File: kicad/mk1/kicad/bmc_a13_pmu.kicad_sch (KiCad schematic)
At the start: 55 parts, among them SW3 PWR_BUT, U25 SY8008A, U26 SY8008A, U3 AXP209

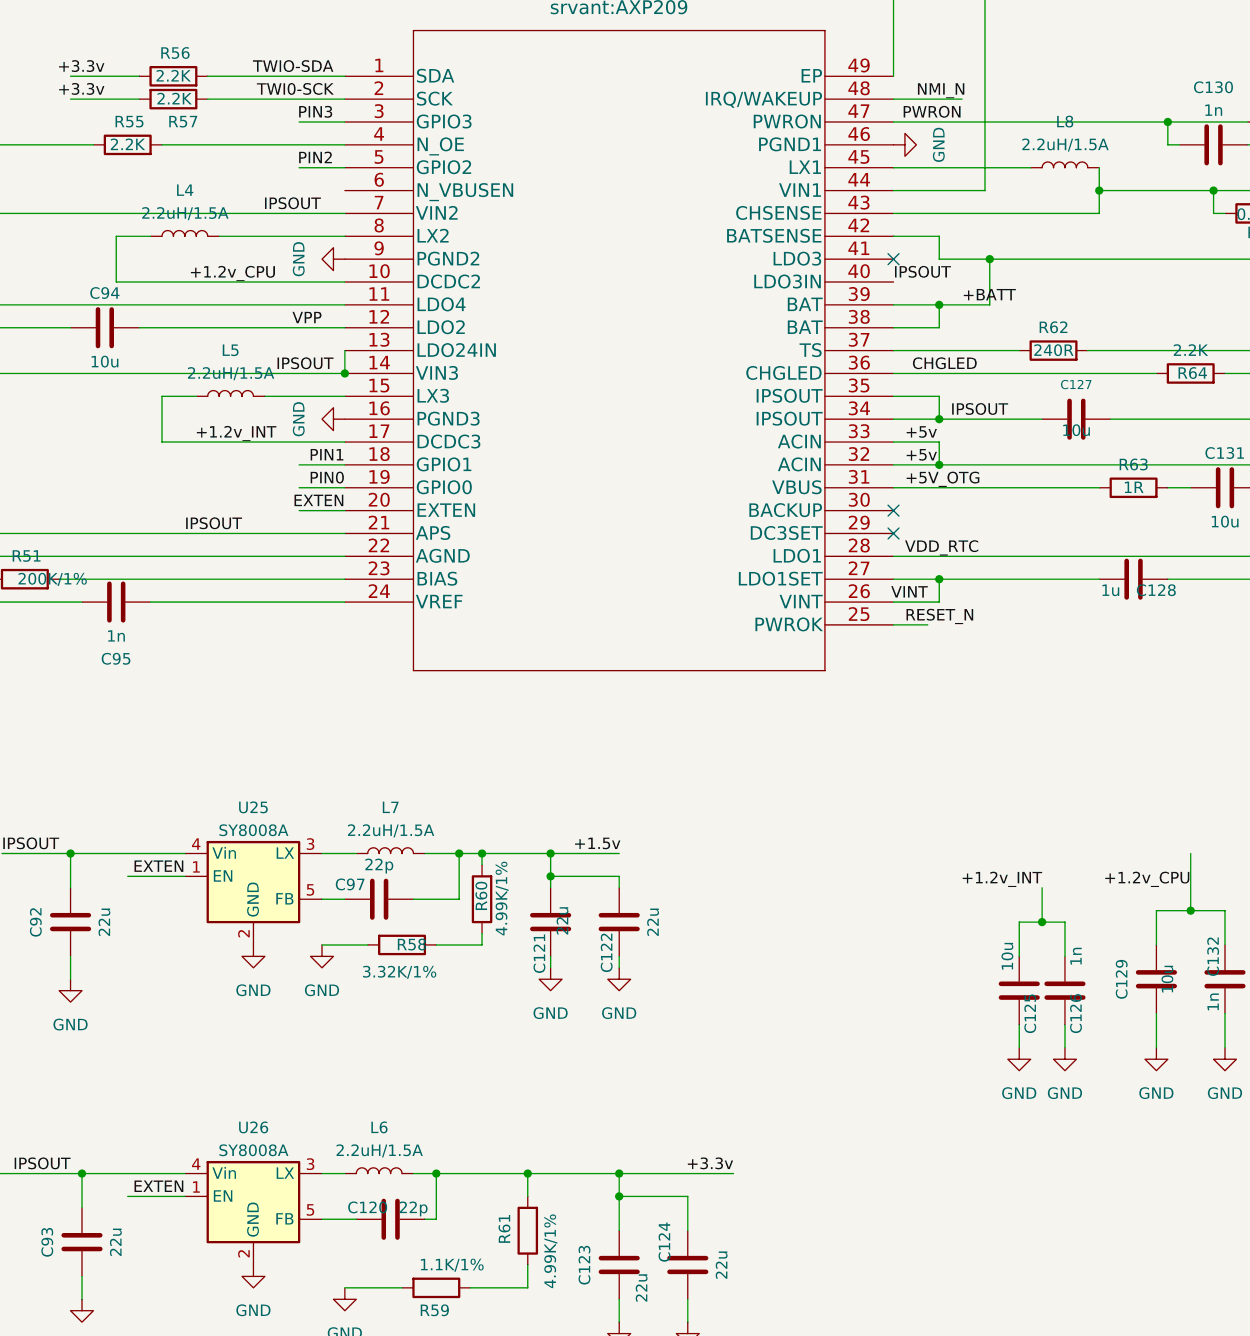
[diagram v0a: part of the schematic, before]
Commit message: work on schematics
* add power rail
* import CM4 related part
* design most of the BMC-PHY part
* create new library/footprint for rp t113-s3 SOM
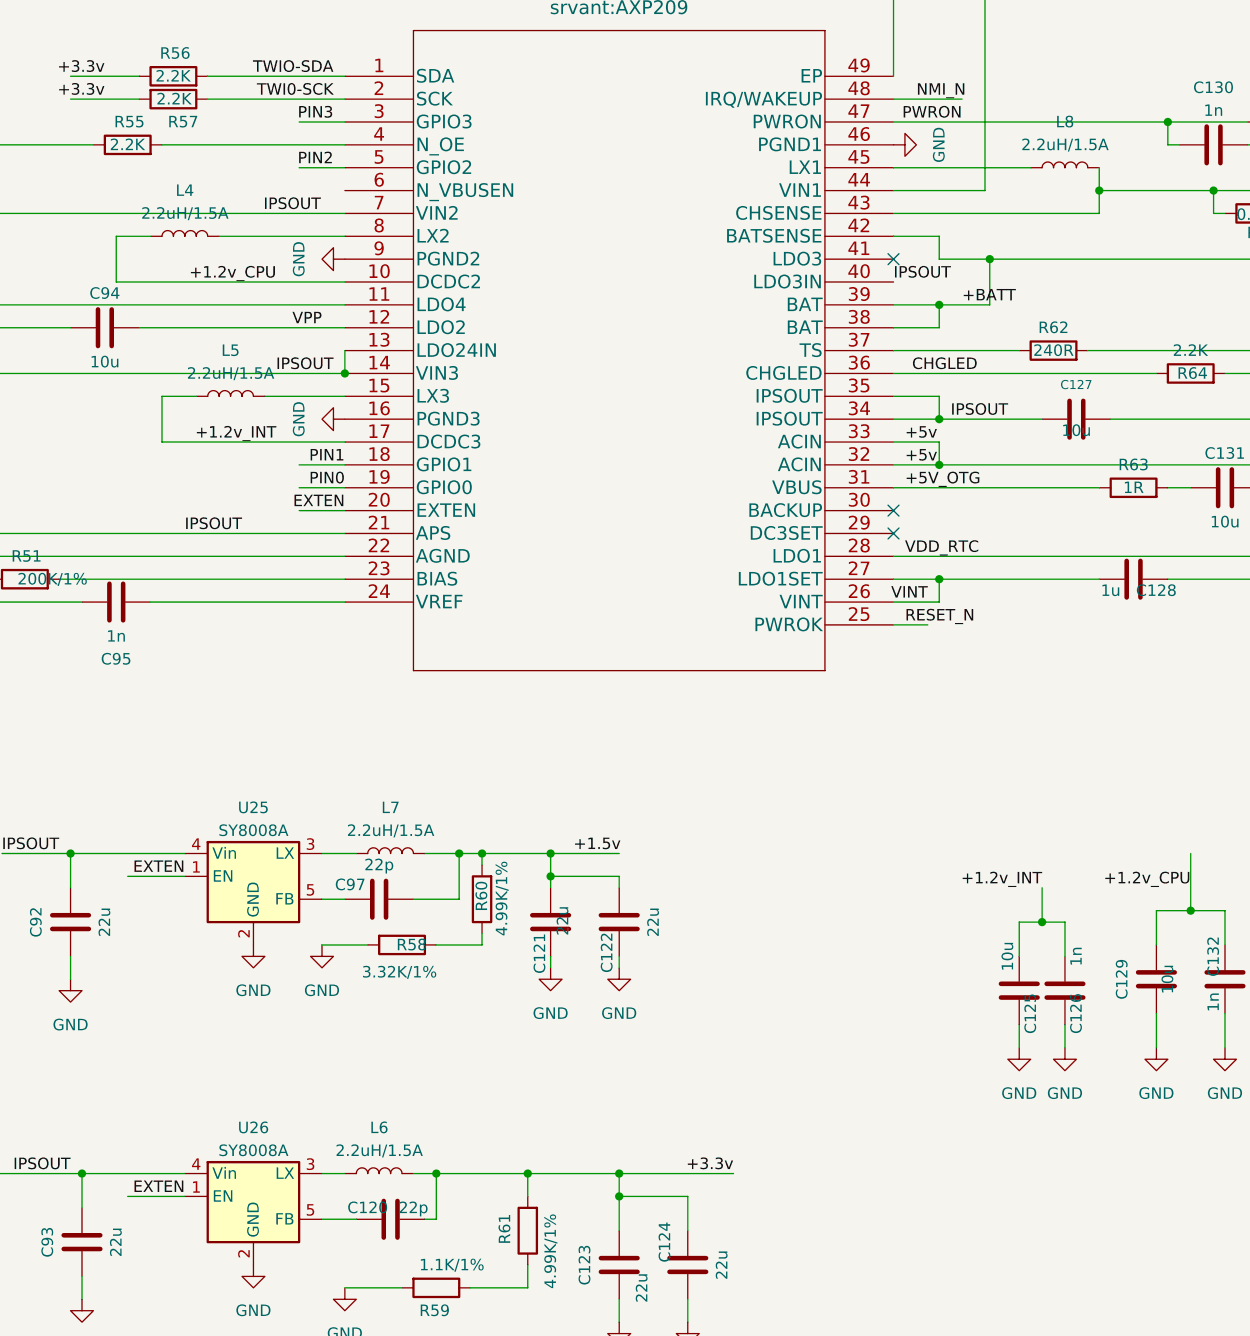
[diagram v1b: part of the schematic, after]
